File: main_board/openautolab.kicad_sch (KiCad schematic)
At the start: 32 parts, among them J1 PIN11, J10 HX711, J11 LCD, J12 OUT+, J13 OUT-, J14 IN+, J15 IN-, J16 PWR_IN, J17 FILTER_PUMP, J18 FILTER_SENSOR, J2 PIN9, J3 PIN10, J4 PIN12, J6 PIN7, J7 PIN8, J8 PUMP, J9 SERVO, K1 FINDER-36.11, K2 FINDER-36.11, SW0 PIN_A0, SW1 PIN_A1, SW2 PIN_A2, SW3 SW_SPDT, U1 TD62064APG, U2 TD62064APG

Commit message: update PCB
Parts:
- removed J12: OUT+, Connector_PinHeader_2.54mm:PinHeader_1x01_P2.54mm_Vertical, symbol Connector_Generic:Conn_01x01
- removed J13: OUT-, Connector_PinHeader_2.54mm:PinHeader_1x01_P2.54mm_Vertical, symbol Connector_Generic:Conn_01x01
- removed J14: IN+, Connector_PinHeader_2.54mm:PinHeader_1x01_P2.54mm_Vertical, symbol Connector_Generic:Conn_01x01
- removed J15: IN-, Connector_PinHeader_2.54mm:PinHeader_1x01_P2.54mm_Vertical, symbol Connector_Generic:Conn_01x01
- removed SW3: SW_SPDT, Button_Switch_THT:SW_Slide_1P2T_CK_OS102011MS2Q, symbol Switch:SW_SPDT
- added C1: C_Polarized, Capacitor_THT:CP_Radial_D10.0mm_P5.00mm, symbol Device:C_Polarized
- added C2: C_Polarized, Capacitor_THT:CP_Radial_D8.0mm_P5.00mm, symbol Device:C_Polarized
- added D6: 1N5822, Diode_THT:D_DO-201AD_P15.24mm_Horizontal, symbol Diode:1N5822
- added L1: L, Inductor_THT:L_Toroid_Vertical_L26.7mm_W14.0mm_P10.16mm_Pulse_D, symbol Device:L
- added NT1: NetTie_2, NetTie:NetTie-2_SMD_Pad2.0mm, symbol Device:NetTie_2
- added SW3: SW_DPST_x2, Connector_PinHeader_2.54mm:PinHeader_1x02_P2.54mm_Vertical, symbol Switch:SW_DPST_x2
- added U3: LM2576T-5, Package_TO_SOT_THT:TO-220-5_Vertical, symbol Regulator_Switching:LM2576T-5
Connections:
- net +12V: now also C2.1, U3.1 (VIN)
- net +5V: now also C1.1, L1.2, U3.4 (FB)
- net GND: now also C1.2, C2.2, D6.2 (A), NT1.1, U3.3 (GND), U3.5 (~{ON}/OFF)
- net GNDPWR: now also NT1.2
- net at J18.2 (Pin_2): now also SW3.2 (B)
- net at D5.2 (A), J17.1 (Pin_1): now also SW3.1 (A)
- new net: D6.1 (K), L1.1, U3.2 (OUT)
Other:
- moved on the sheet: J16, J18

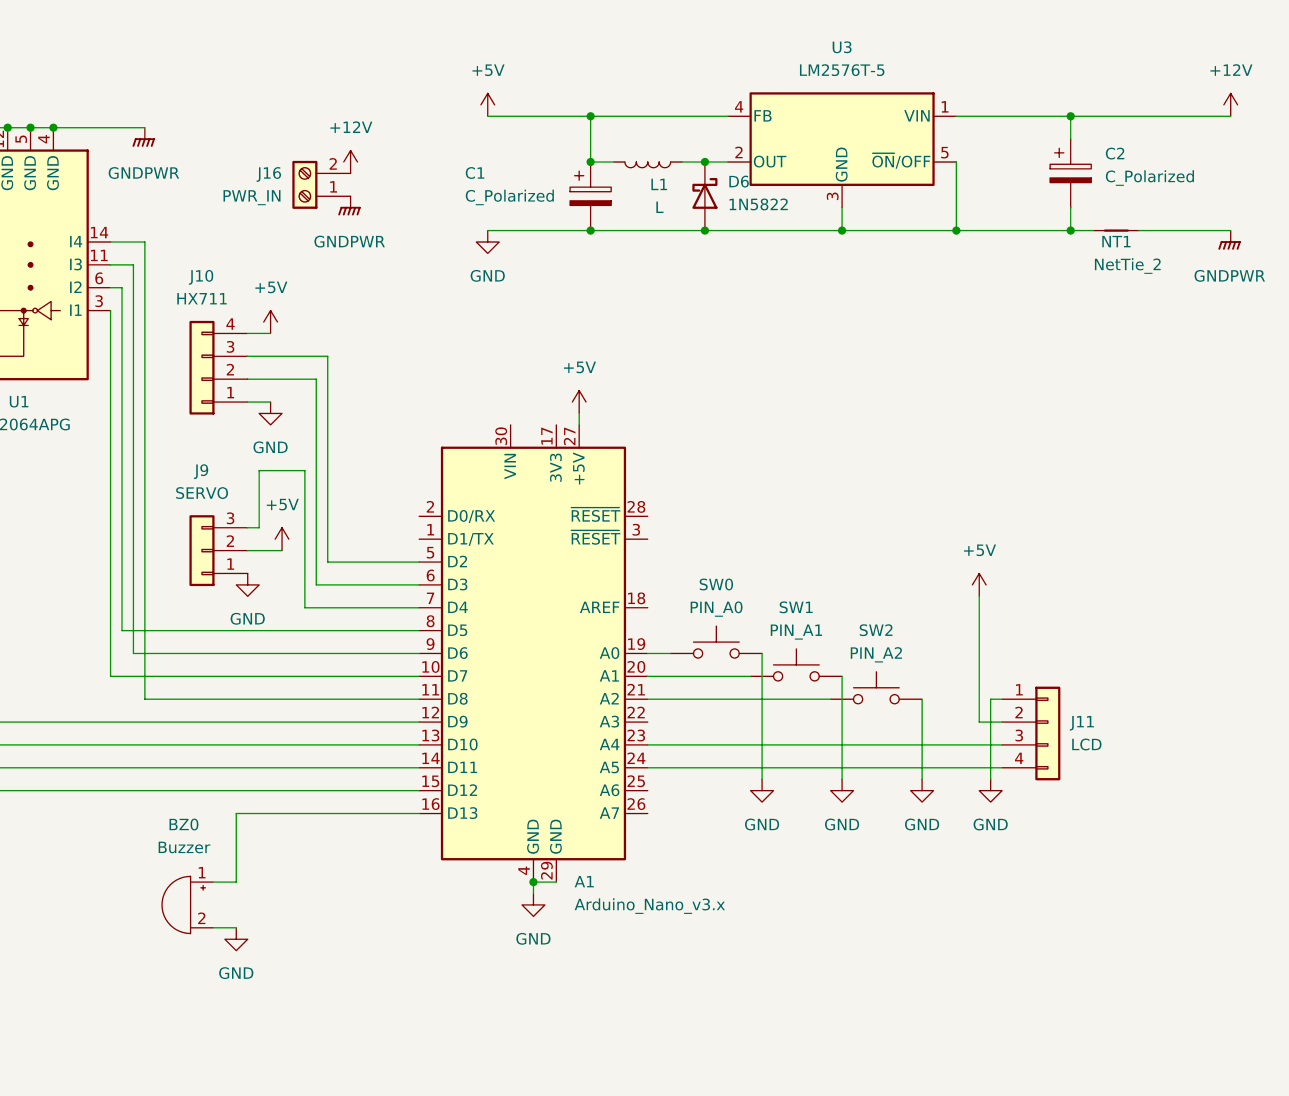
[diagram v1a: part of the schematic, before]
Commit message: update schematic add power switch
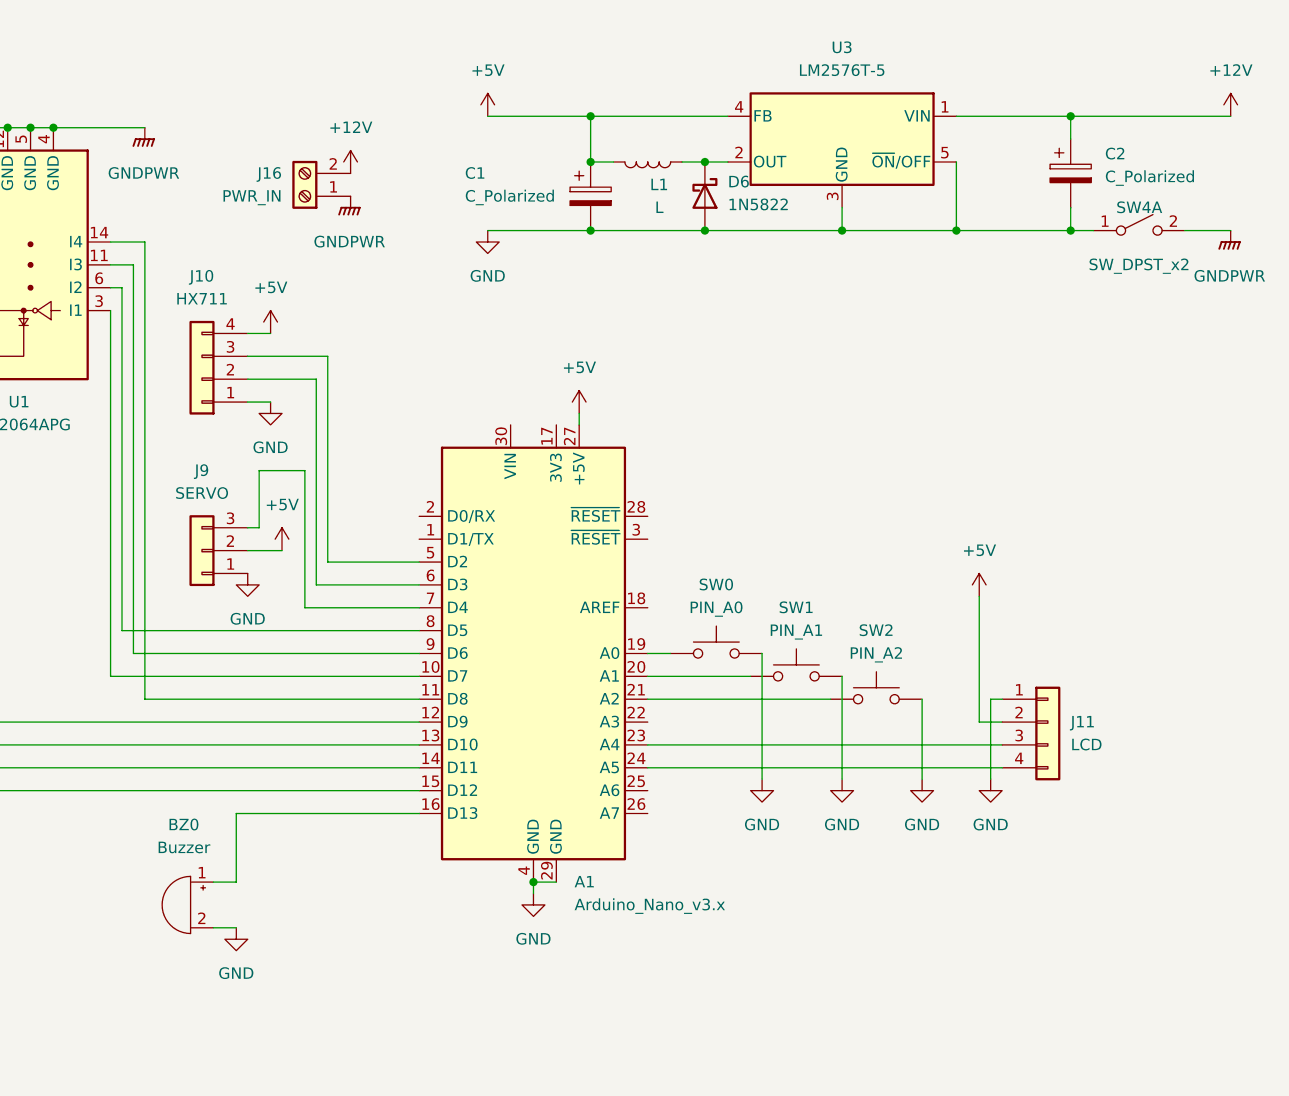
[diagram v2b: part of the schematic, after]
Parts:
- removed NT1: NetTie_2, NetTie:NetTie-2_SMD_Pad2.0mm, symbol Device:NetTie_2
- added SW4: SW_DPST_x2, Connector_PinHeader_2.54mm:PinHeader_1x02_P2.54mm_Vertical, symbol Switch:SW_DPST_x2
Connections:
- net GND: now also SW4.1 (A)
- net GNDPWR: now also SW4.2 (B)

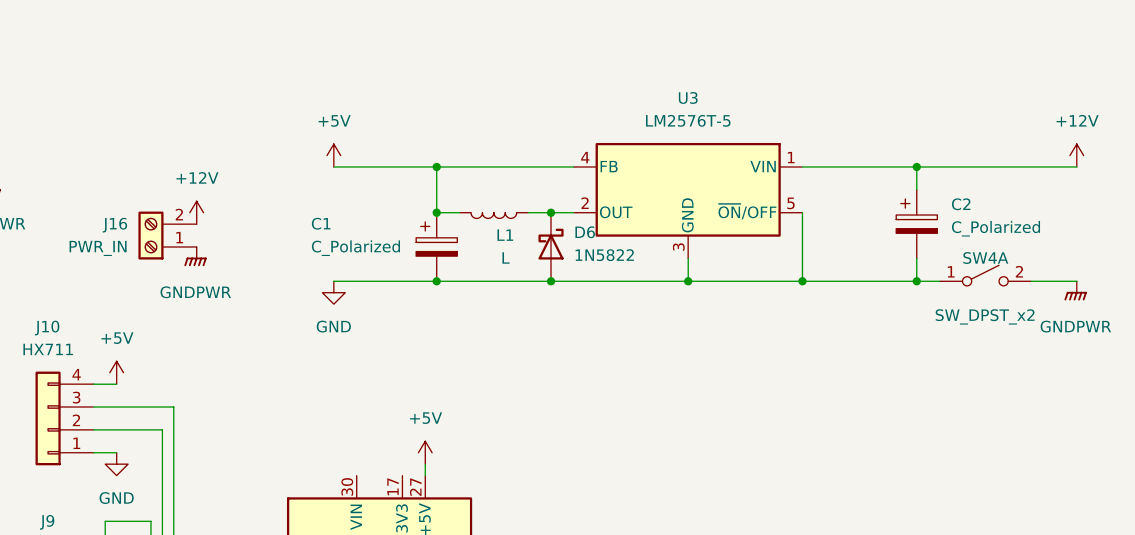
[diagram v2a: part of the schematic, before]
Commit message: fixed power switch on board
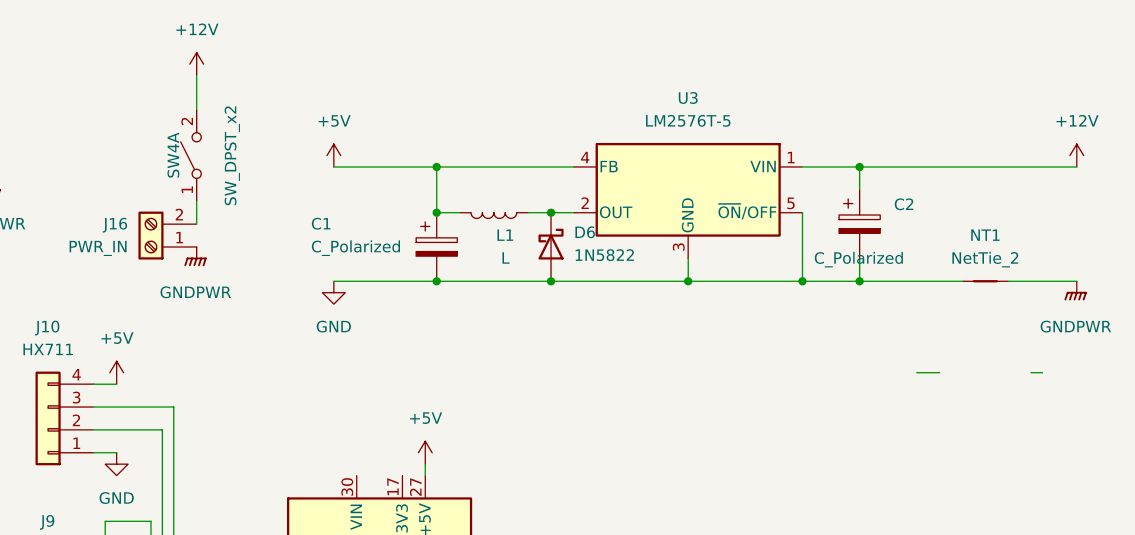
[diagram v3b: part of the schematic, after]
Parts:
- added NT1: NetTie_2, NetTie:NetTie-2_SMD_Pad2.0mm, symbol Device:NetTie_2
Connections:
- net +12V: now also SW4.2 (B); no longer J16.2 (Pin_2)
- net GND: now also NT1.1; no longer SW4.1 (A)
- net GNDPWR: now also NT1.2; no longer SW4.2 (B)
- new net: J16.2 (Pin_2), SW4.1 (A)
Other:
- moved on the sheet: C2, SW4A
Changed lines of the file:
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@@
   (junction (at 102.87 77.47) (diameter 0) (color 0 0 0 0)
   )
-  (junction (at 243.84 40.64) (diameter 0) (color 0 0 0 0)
-  )
   (junction (at 50.8 148.59) (diameter 0) (color 0 0 0 0)
   )
@@
   (junction (at 203.2 33.02) (diameter 0) (color 0 0 0 0)
   )
+  (junction (at 237.49 27.94) (diameter 0) (color 0 0 0 0)
+  )
   (junction (at 190.5 33.02) (diameter 0) (color 0 0 0 0)
   )
-  (junction (at 243.84 27.94) (diameter 0) (color 0 0 0 0)
-  )
   (junction (at 97.79 77.47) (diameter 0) (color 0 0 0 0)
   )
@@
   (junction (at 218.44 40.64) (diameter 0) (color 0 0 0 0)
   )
+  (junction (at 237.49 40.64) (diameter 0) (color 0 0 0 0)
+  )
   (wire (pts (xy 81.28 46.99) (xy 82.55 46.99))
     (stroke (width 0) (type default))
@@
     (stroke (width 0) (type default))
   )
-  (wire (pts (xy 243.84 27.94) (xy 261.62 27.94))
+  (wire (pts (xy 237.49 27.94) (xy 261.62 27.94))
     (stroke (width 0) (type default))
   )
@@
     (stroke (width 0) (type default))
   )
-  (wire (pts (xy 231.14 40.64) (xy 243.84 40.64))
+  (wire (pts (xy 231.14 40.64) (xy 237.49 40.64))
     (stroke (width 0) (type default))
   )
@@
     (stroke (width 0) (type default))
   )
-  (wire (pts (xy 243.84 27.94) (xy 243.84 30.48))
+  (wire (pts (xy 237.49 27.94) (xy 237.49 30.48))
     (stroke (width 0) (type default))
   )
@@
     (stroke (width 0) (type default))
   )
+  (wire (pts (xy 163.83 17.78) (xy 163.83 21.59))
+    (stroke (width 0) (type default))
+  )
   (wire (pts (xy 80.01 90.17) (xy 88.9 90.17))
     (stroke (width 0) (type default))
@@
     (stroke (width 0) (type default))
   )
-  (wire (pts (xy 243.84 38.1) (xy 243.84 40.64))
+  (wire (pts (xy 237.49 38.1) (xy 237.49 40.64))
     (stroke (width 0) (type default))
   )
@@
     (stroke (width 0) (type default))
   )
-  (wire (pts (xy 243.84 40.64) (xy 246.38 40.64))
+  (wire (pts (xy 243.84 50.8) (xy 246.38 50.8))
     (stroke (width 0) (type default))
   )
@@
     (stroke (width 0) (type default))
   )
-  (wire (pts (xy 231.14 27.94) (xy 243.84 27.94))
+  (wire (pts (xy 231.14 27.94) (xy 237.49 27.94))
     (stroke (width 0) (type default))
   )
@@
     (stroke (width 0) (type default))
   )
+  (wire (pts (xy 163.83 31.75) (xy 163.83 34.29))
+    (stroke (width 0) (type default))
+  )
   (wire (pts (xy 160.02 80.01) (xy 171.45 80.01))
     (stroke (width 0) (type default))
@@
     (stroke (width 0) (type default))
   )
+  (wire (pts (xy 254 40.64) (xy 261.62 40.64))
+    (stroke (width 0) (type default))
+  )
   (wire (pts (xy 105.41 54.61) (xy 105.41 57.15))
     (stroke (width 0) (type default))
@@
     (stroke (width 0) (type default))
   )
-  (wire (pts (xy 256.54 40.64) (xy 261.62 40.64))
+  (wire (pts (xy 256.54 50.8) (xy 257.81 50.8))
     (stroke (width 0) (type default))
   )
@@
   )
   (wire (pts (xy 109.22 31.75) (xy 109.22 39.37))
+    (stroke (width 0) (type default))
+  )
+  (wire (pts (xy 237.49 40.64) (xy 248.92 40.64))
     (stroke (width 0) (type default))
   )
@@
     )
   )
+  (symbol (lib_id "Device:NetTie_2") (at 251.46 40.64 0) (unit 1)
+    (in_bom no) (on_board yes) (dnp no) (fields_autoplaced)
+    (property "Reference" "NT1" (at 251.46 35.56 0)
+      (effects (font (size 1.27 1.27)))
+    )
+    (property "Value" "NetTie_2" (at 251.46 38.1 0)
+      (effects (font (size 1.27 1.27)))
+    )
+    (property "Footprint" "NetTie:NetTie-2_SMD_Pad2.0mm" (at 251.46 40.64 0)
+      (effects (font (size 1.27 1.27)) hide)
+    )
+    (property "Datasheet" "~" (at 251.46 40.64 0)
+      (effects (font (size 1.27 1.27)) hide)
+    )
+    (pin "1")
+    (pin "2")
+    (instances
+      (project "openautolab"
+        (path "/cfdd5521-a8c1-4ce8-a79b-bc50281bd389"
+          (reference "NT1") (unit 1)
+        )
+      )
+    )
+  )
   (symbol (lib_id "power:GNDPWR") (at 99.06 63.5 0) (unit 1)
     (in_bom yes) (on_board yes) (dnp no) (fields_autoplaced)
@@
     )
   )
-  (symbol (lib_id "power:+12V") (at 163.83 34.29 0) (unit 1)
-    (in_bom yes) (on_board yes) (dnp no) (fields_autoplaced)
-    (property "Reference" "#PWR0136" (at 163.83 38.1 0)
-      (effects (font (size 1.27 1.27)) hide)
-    )
-    (property "Value" "+12V" (at 163.83 29.21 0)
-      (effects (font (size 1.27 1.27)))
-    )
-    (property "Footprint" "" (at 163.83 34.29 0)
-      (effects (font (size 1.27 1.27)) hide)
-    )
-    (property "Datasheet" "" (at 163.83 34.29 0)
+  (symbol (lib_id "power:+12V") (at 163.83 17.78 0) (unit 1)
+    (in_bom yes) (on_board yes) (dnp no)
+    (property "Reference" "#PWR0136" (at 163.83 21.59 0)
+      (effects (font (size 1.27 1.27)) hide)
+    )
+    (property "Value" "+12V" (at 163.83 12.7 0)
+      (effects (font (size 1.27 1.27)))
+    )
+    (property "Footprint" "" (at 163.83 17.78 0)
+      (effects (font (size 1.27 1.27)) hide)
+    )
+    (property "Datasheet" "" (at 163.83 17.78 0)
       (effects (font (size 1.27 1.27)) hide)
     )
@@
     )
   )
-  (symbol (lib_id "Device:C_Polarized") (at 243.84 34.29 0) (unit 1)
-    (in_bom yes) (on_board yes) (dnp no) (fields_autoplaced)
-    (property "Reference" "C2" (at 247.65 32.1309 0)
-      (effects (font (size 1.27 1.27)) (justify left))
-    )
-    (property "Value" "C_Polarized" (at 247.65 34.6709 0)
-      (effects (font (size 1.27 1.27)) (justify left))
-    )
-    (property "Footprint" "Capacitor_THT:CP_Radial_D8.0mm_P5.00mm" (at 244.8052 38.1 0)
-      (effects (font (size 1.27 1.27)) hide)
-    )
-    (property "Datasheet" "~" (at 243.84 34.29 0)
+  (symbol (lib_id "Device:C_Polarized") (at 237.49 34.29 0) (unit 1)
+    (in_bom yes) (on_board yes) (dnp no)
+    (property "Reference" "C2" (at 241.3 32.1309 0)
+      (effects (font (size 1.27 1.27)) (justify left))
+    )
+    (property "Value" "C_Polarized" (at 232.41 38.1 0)
+      (effects (font (size 1.27 1.27)) (justify left))
+    )
+    (property "Footprint" "Capacitor_THT:CP_Radial_D8.0mm_P5.00mm" (at 238.4552 38.1 0)
+      (effects (font (size 1.27 1.27)) hide)
+    )
+    (property "Datasheet" "~" (at 237.49 34.29 0)
       (effects (font (size 1.27 1.27)) hide)
     )
@@
     )
   )
-  (symbol (lib_id "Switch:SW_DPST_x2") (at 251.46 40.64 0) (unit 1)
+  (symbol (lib_id "Switch:SW_DPST_x2") (at 163.83 26.67 90) (unit 1)
     (in_bom yes) (on_board yes) (dnp no)
-    (property "Reference" "SW4" (at 251.46 38.1 0)
-      (effects (font (size 1.27 1.27)))
-    )
-    (property "Value" "SW_DPST_x2" (at 251.46 44.45 0)
-      (effects (font (size 1.27 1.27)))
-    )
-    (property "Footprint" "Connector_PinHeader_2.54mm:PinHeader_1x02_P2.54mm_Vertical" (at 251.46 40.64 0)
-      (effects (font (size 1.27 1.27)) hide)
-    )
-    (property "Datasheet" "~" (at 251.46 40.64 0)
-      (effects (font (size 1.27 1.27)) hide)
-    )
+    (property "Reference" "SW4" (at 161.29 26.67 0)
+      (effects (font (size 1.27 1.27)))
+    )
+    (property "Value" "SW_DPST_x2" (at 167.64 26.67 0)
+      (effects (font (size 1.27 1.27)))
+    )
+    (property "Footprint" "Connector_PinHeader_2.54mm:PinHeader_1x02_P2.54mm_Vertical" (at 163.83 26.67 0)
+      (effects (font (size 1.27 1.27)) hide)
+    )
+    (property "Datasheet" "~" (at 163.83 26.67 0)
+      (effects (font (size 1.27 1.27)) hide)
+    )
